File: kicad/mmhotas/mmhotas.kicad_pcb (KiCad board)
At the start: 2 copper layers, 72.1 x 19.6 mm, 30 parts, among them J1 Conn_01x03_Male, J2 Conn_01x03_Male, J3 Conn_01x03_Male, J4 Conn_01x05_Male, J5 Conn_01x04_Male, J6 Conn_01x03_Male, J7 Conn_01x03_Male, J8 Conn_01x04_Male

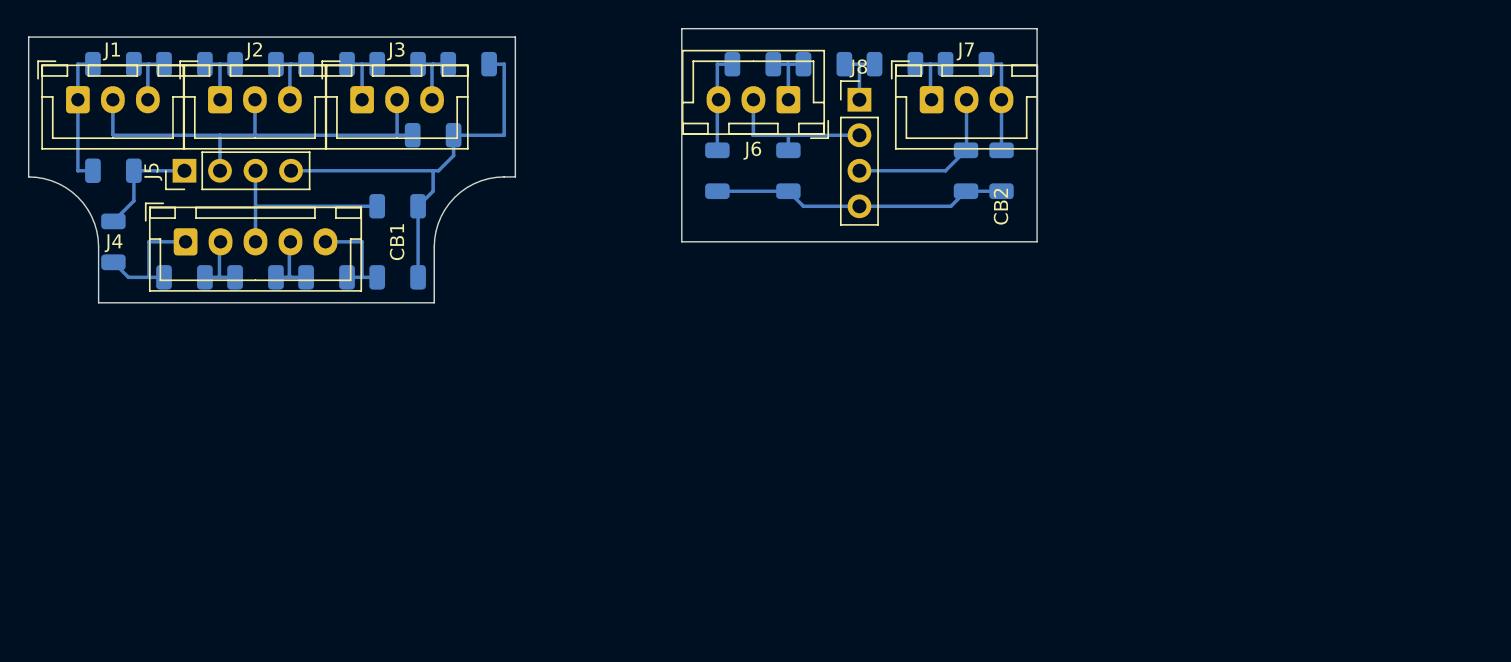
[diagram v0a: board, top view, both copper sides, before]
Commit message: Designed connector board Backups removed
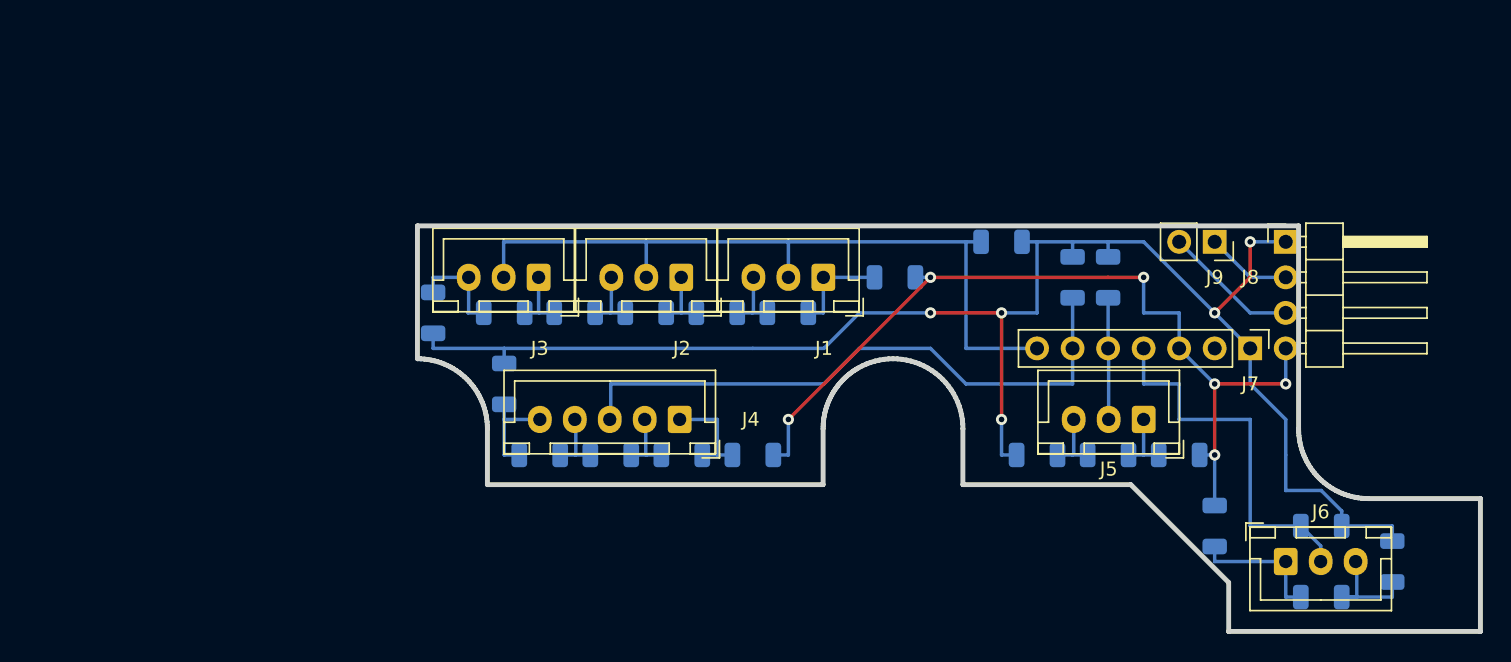
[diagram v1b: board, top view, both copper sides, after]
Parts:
- removed the J5 at (53.3, 35.6)
- added J7: Conn_01x07_Male, Connector_PinHeader_2.54mm:PinHeader_1x07_P2.54mm_Vertical, F.Cu at (129.5, 48.3)
- added J9: Conn_01x02_Female, Connector_PinSocket_2.54mm:PinSocket_1x02_P2.54mm_Vertical, F.Cu at (127.0, 40.6)
- J8: footprint Connector_PinHeader_2.54mm:PinHeader_1x04_P2.54mm_Vertical -> Connector_PinHeader_2.54mm:PinHeader_1x04_P2.54mm_Horizontal
- moved R2 56.4 mm to (104.1, 43.2)
- moved J1 54.8 mm to (99.0, 43.2), turned to 180 degrees
- moved R3 51.4 mm to (96.5, 45.7), turned to 180 degrees
- moved R14 48.5 mm to (116.8, 43.2), turned to 90 degrees
- moved R9 48.2 mm to (94.0, 55.9), turned to 180 degrees
- moved R20 45.8 mm to (134.6, 66.0)
- moved R4 42.0 mm to (91.4, 45.7), turned to 180 degrees
- moved J6 41.6 mm to (132.1, 63.5)
- moved R1 41.3 mm to (111.8, 40.6)
- moved R19 40.2 mm to (127.0, 61.0), turned to -90 degrees
- moved R21 39.5 mm to (139.7, 63.5), turned to 90 degrees
- moved R10 37.8 mm to (88.9, 55.9), turned to 180 degrees
- moved R15 37.8 mm to (124.5, 55.9)
- moved R16 37.8 mm to (119.4, 55.9)
- moved J4 37.5 mm to (88.7, 53.3), turned to 180 degrees
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- renumbered J6 to J5, J7 to J6
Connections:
- J5 pad 2: Net-(J6-Pad2) -> Net-(J5-Pad2)
- J6 pad 2: Net-(J7-Pad2) -> Net-(J6-Pad2)
- J8 pad 1: Net-(J8-Pad1) -> Net-(J7-Pad1)
- J8 pad 2: Net-(J6-Pad2) -> Net-(J8-Pad2)
- J8 pad 3: Net-(J7-Pad2) -> Net-(J8-Pad3)
- J8 pad 4: Net-(J8-Pad4) -> Net-(J7-Pad3)
- R1 pad 2: Net-(J5-Pad4) -> Net-(J7-Pad1)
- R13 pad 2: Net-(J5-Pad4) -> Net-(J7-Pad1)
- R14 pad 2: Net-(J5-Pad4) -> Net-(J7-Pad1)
- R15 pad 1: Net-(J8-Pad1) -> Net-(J7-Pad3)
- R17 pad 2: Net-(J8-Pad4) -> Net-(J7-Pad1)
- R18 pad 1: Net-(J6-Pad2) -> Net-(J5-Pad2)
- R18 pad 2: Net-(J8-Pad4) -> Net-(J7-Pad1)
- R19 pad 1: Net-(J8-Pad1) -> Net-(J7-Pad3)
- R2 pad 1: Net-(J5-Pad1) (its old number) -> Net-(J7-Pad3)
- R21 pad 2: Net-(J8-Pad4) -> Net-(J7-Pad1)
- R22 pad 1: Net-(J7-Pad2) -> Net-(J6-Pad2)
- R22 pad 2: Net-(J8-Pad4) -> Net-(J7-Pad1)
- R8 pad 2: Net-(J5-Pad4) -> Net-(J7-Pad1)
- R9 pad 1: Net-(J5-Pad1) (its old number) -> Net-(J7-Pad3)
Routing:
- net Net-(J7-Pad1): track 0.00 -> 114.6 mm, vias 0 -> 5
- net Net-(J7-Pad3): track 0.00 -> 62.9 mm, vias 0 -> 6
- net Net-(J5-Pad4): track 31.4 -> 0.00 mm
- net Net-(J4-Pad3): track 13.9 -> 43.8 mm
- net Net-(J1-Pad2): track 31.6 -> 54.4 mm
- net Net-(J8-Pad4): track 21.2 -> 0.00 mm
- net Net-(J6-Pad2): track 11.3 -> 27.1 mm
- net Net-(J7-Pad2): track 11.9 -> 0.00 mm
- net Net-(J8-Pad3): track 0.00 -> 9.72 mm
- net Net-(J5-Pad2): track 0.00 -> 8.71 mm
- net Net-(J5-Pad1) (its old number): track 7.84 -> 0.00 mm
- net Net-(J8-Pad2): track 0.00 -> 6.13 mm
- net Net-(J6-Pad1): track 4.69 -> 9.78 mm
- net Net-(J8-Pad1): track 4.70 -> 0.00 mm
- net Net-(J3-Pad3): track 4.73 -> 7.25 mm
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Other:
- board size 72.1 x 19.6 mm -> 76 x 29 mm
- board text removed: "CB1"
- board text removed: "CB2"
